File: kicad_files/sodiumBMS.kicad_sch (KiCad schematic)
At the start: 22 parts, among them J3 USB_C_Receptacle_USB2.0_16P, Q4 AO3400A, SW2 BOOT, SW3 RESET, U1 STM32F446RETx, U4 LM3940, Y1 8MHz or 16 Mhz

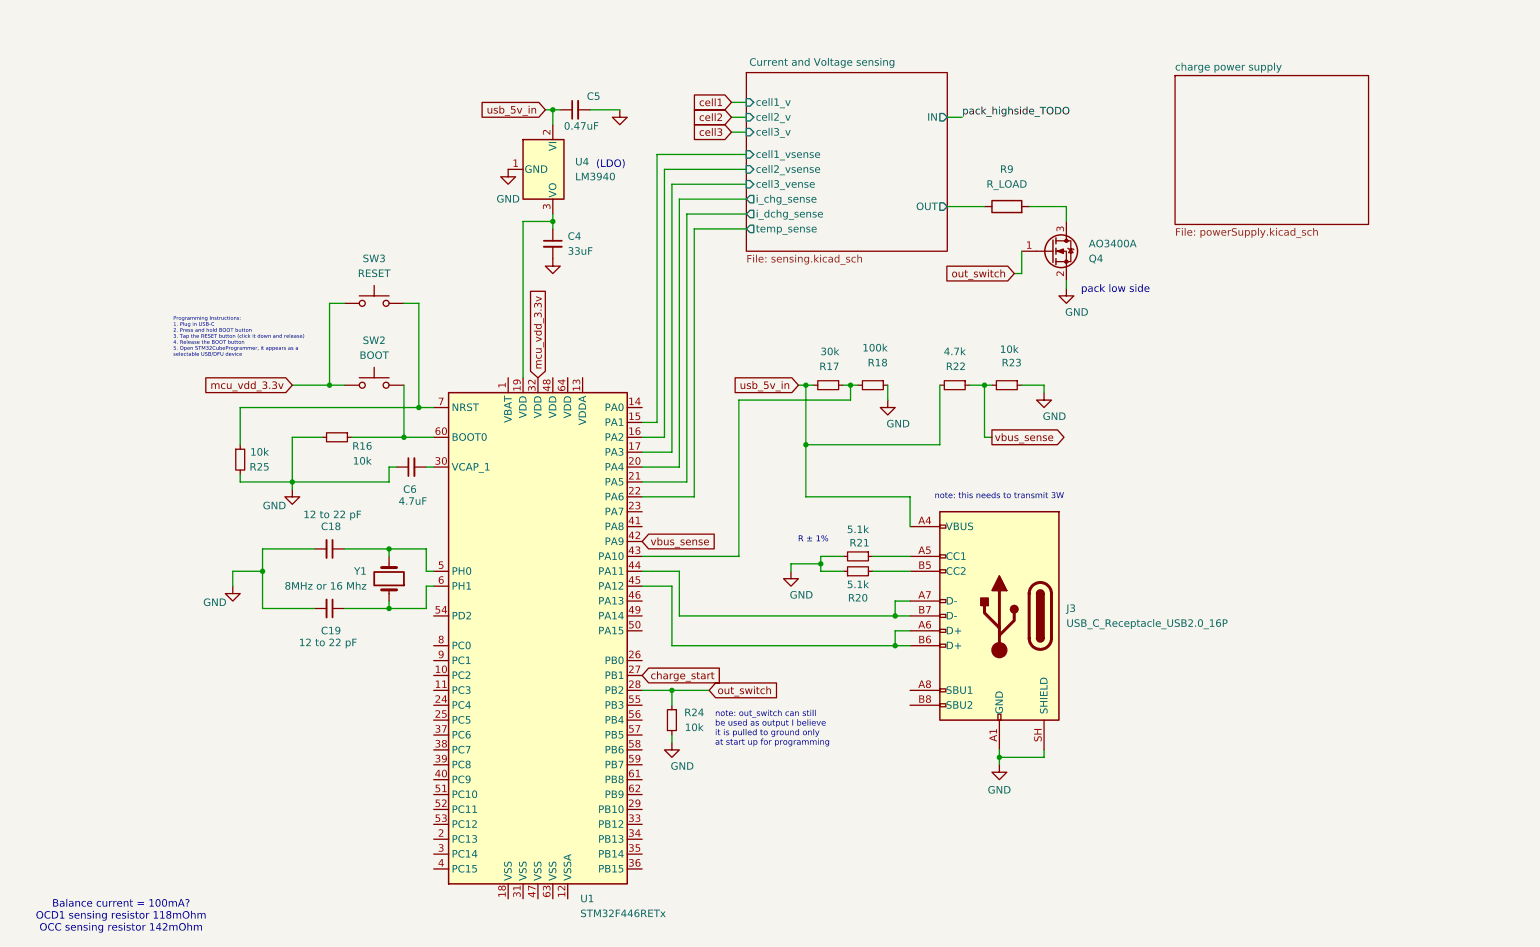
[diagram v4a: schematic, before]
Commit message: Add 3S battery configuration
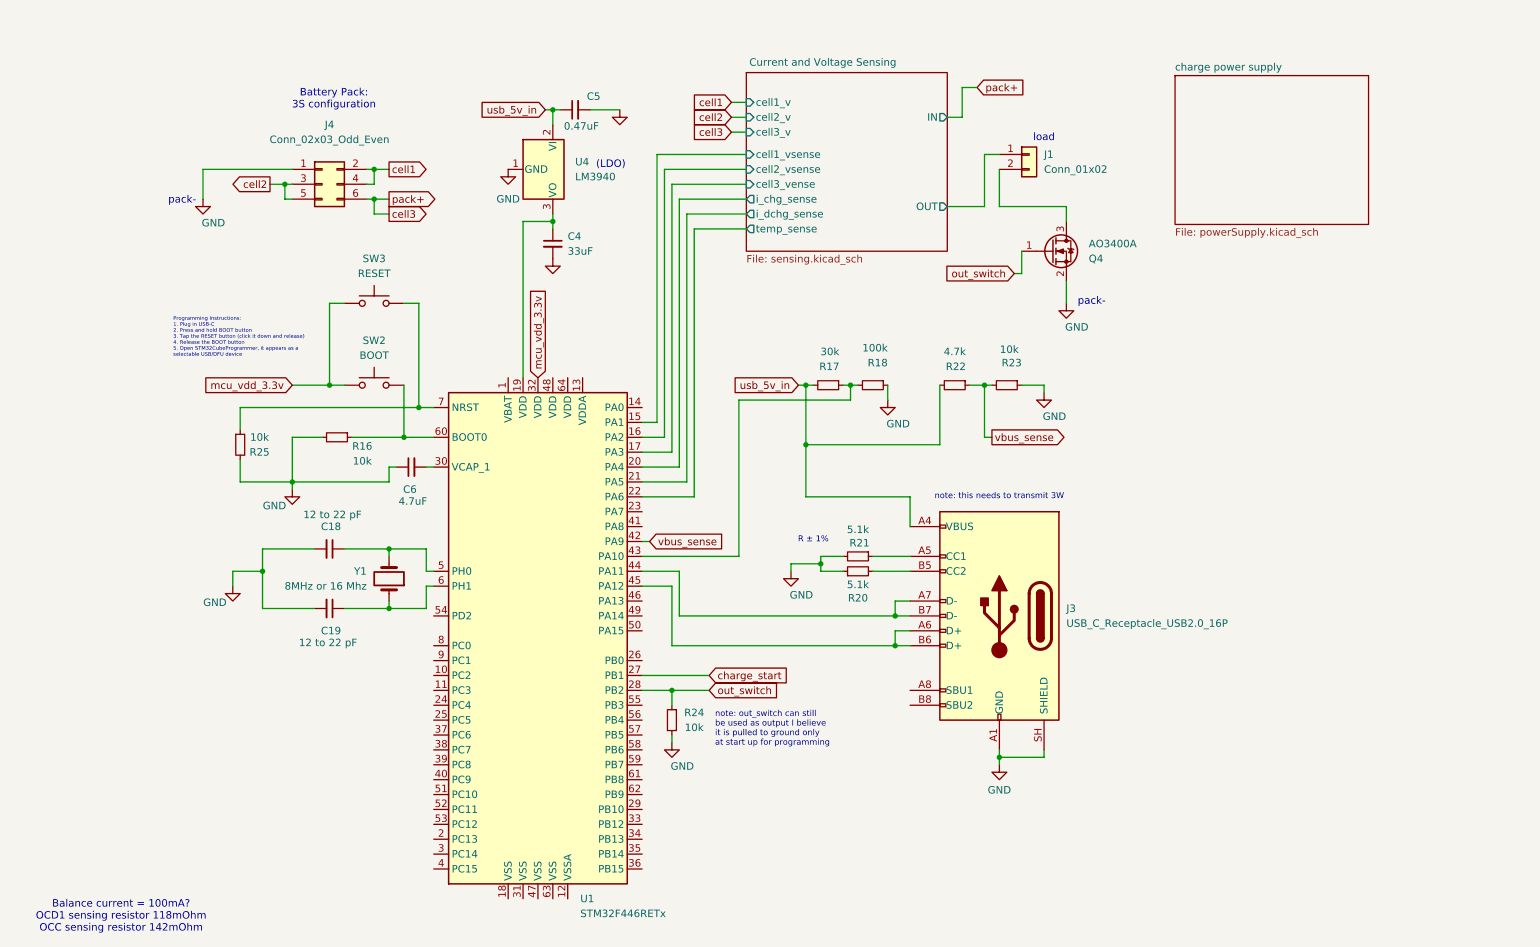
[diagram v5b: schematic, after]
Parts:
- removed R9: R_LOAD, symbol Device:R
- added J1: Conn_01x02, symbol Connector_Generic:Conn_01x02
- added J4: Conn_02x03_Odd_Even, symbol Connector_Generic:Conn_02x03_Odd_Even
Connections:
- net Current and Voltage Sensing/OUT: now also J1.1 (Pin_1)
- net GND: now also J4.1 (Pin_1)
- net cell1: now also J4.2 (Pin_2), J4.4 (Pin_4)
- net cell2: now also J4.3 (Pin_3), J4.5 (Pin_5)
- net cell3: now also J4.6 (Pin_6)
- net at Q4.3 (D): now also J1.2 (Pin_2)
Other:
- sheet Current and Voltage sensing renamed Current and Voltage Sensing
- note added: "Battery Pack: 3S configuration"
- note added: "load"
- note added: "pack-"
- note removed: "pack low side"
- moved on the sheet: R25

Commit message: Add better comment for battery config
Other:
- note added: "Battery Pack: 3S configuration - cell1 + + cell2 - - cell3 +"
- note removed: "Battery Pack: 3S configuration"
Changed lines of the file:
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@@
 		)
 	)
-	(text "Battery Pack:\n3S configuration"
+	(text "Battery Pack:\n3S configuration\n\n- cell1 +\n+ cell2 -\n- cell3 +"
 		(exclude_from_sim no)
-		(at 80.772 27.432 0)
+		(at 80.01 23.876 0)
 		(effects
 			(font

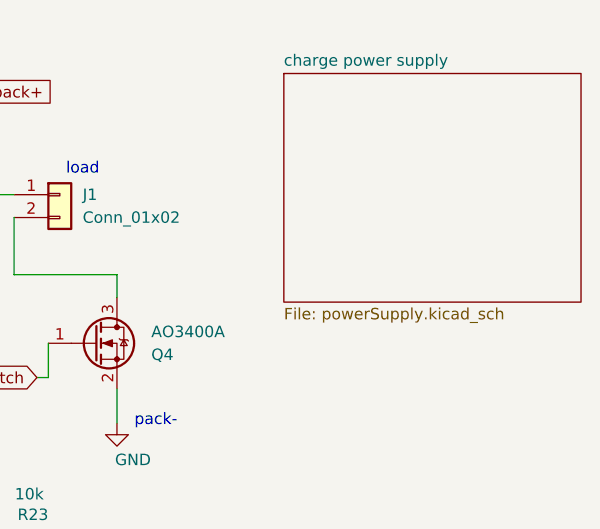
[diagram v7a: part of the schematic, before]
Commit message: Remove power supply and add charging schematic instead
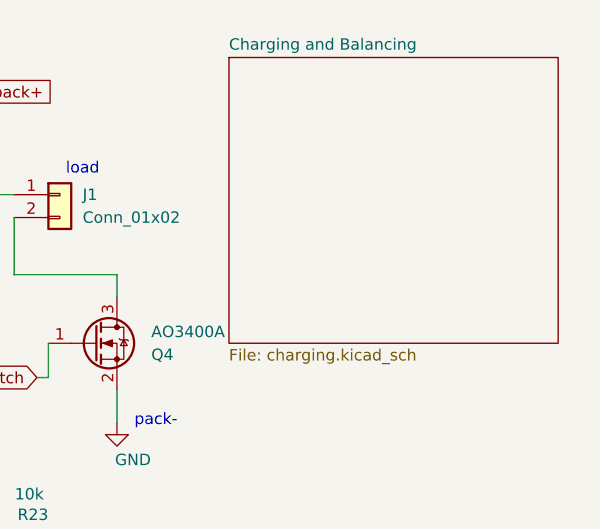
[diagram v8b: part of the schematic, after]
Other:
- removed sheet charge power supply
- added sheet Charging and Balancing (charging.kicad_sch)
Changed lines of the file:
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@@
 	(version 20260306)
 	(generator "eeschema")
-	(generator_version "10.99")
+	(generator_version "10.0")
 	(paper "A4")
 	(text "Programming Instructions:\n1. Plug in USB-C\n2. Press and hold BOOT button\n3. Tap the RESET button (click it down and release)\n4. Release the BOOT button\n5. Open STM32CubeProgrammer, it appears as a\nselectable USB/DFU device"
@@
 	)
 	(sheet
-		(at 224.282 23.368)
-		(size 33.02 25.4)
+		(at 218.186 21.59)
+		(size 36.576 31.75)
 		(exclude_from_sim no)
 		(in_bom yes)
 		(on_board yes)
 		(dnp no)
+		(fields_autoplaced yes)
 		(stroke
 			(width 0.1524)
@@
 			(color 0 0 0 0)
 		)
-		(property "Sheetname" "charge power supply"
-			(at 224.282 22.6564 0)
+		(property "Sheetname" "Charging and Balancing"
+			(at 218.186 20.8784 0)
 			(show_name no)
 			(do_not_autoplace no)
@@
 			)
 		)
-		(property "Sheetfile" "powerSupply.kicad_sch"
-			(at 224.282 49.3526 0)
+		(property "Sheetfile" "charging.kicad_sch"
+			(at 218.186 53.9246 0)
 			(show_name no)
 			(do_not_autoplace no)
